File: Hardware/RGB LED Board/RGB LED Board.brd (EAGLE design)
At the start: 38.1 x 18.7 mm, 9 parts, among them U1 WS2801

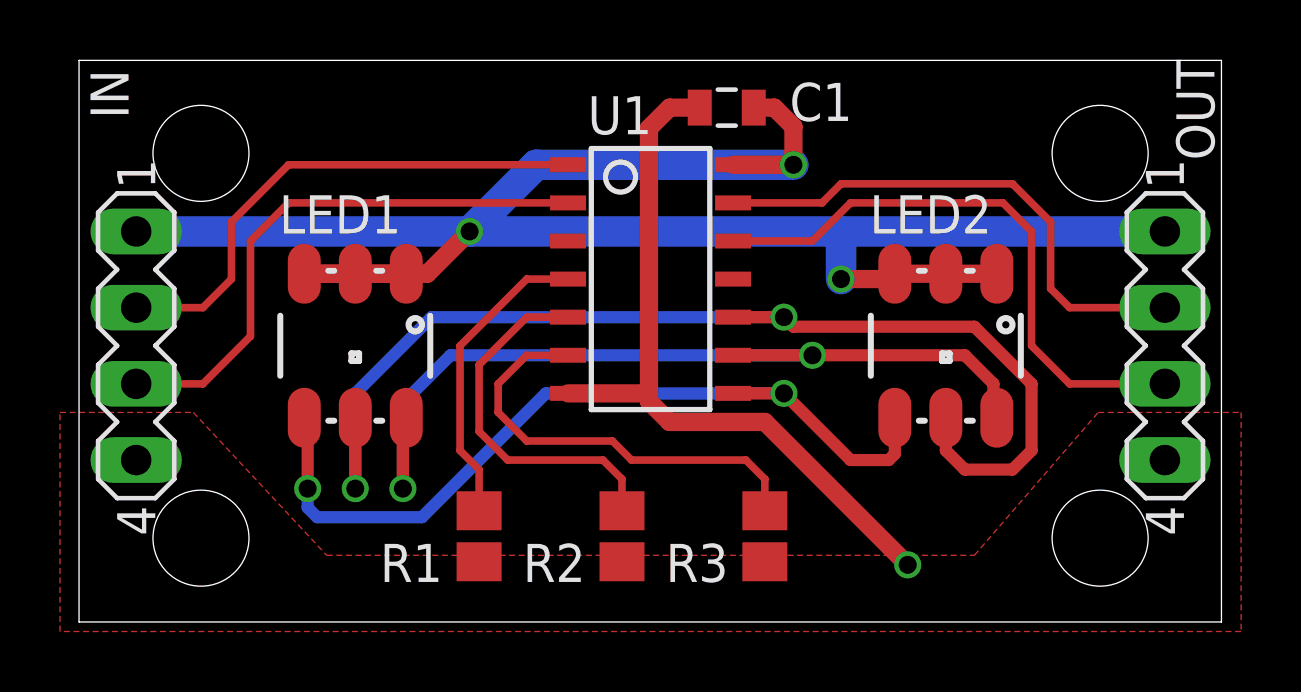
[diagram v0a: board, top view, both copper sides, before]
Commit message: changed LED to CLY6D-FKC-CK1N1D1BB7D3D3
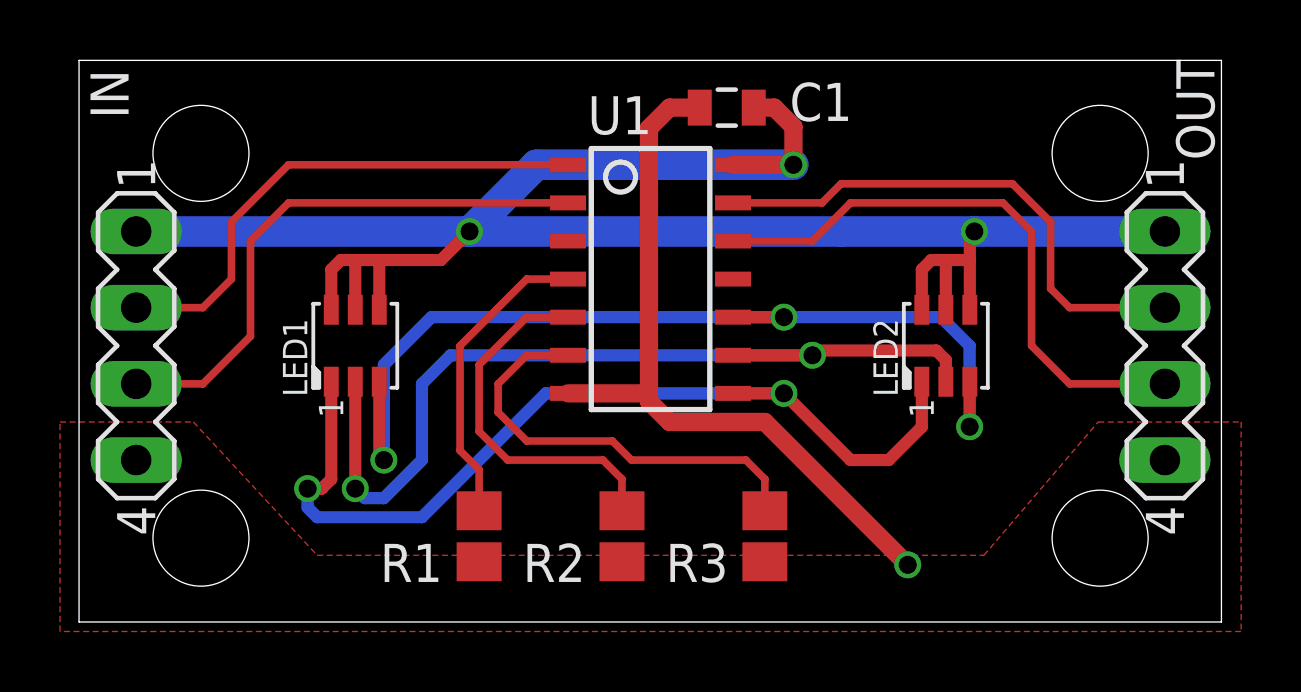
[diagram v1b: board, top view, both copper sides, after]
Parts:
- LED1, LED2: value LED-TRICOLOR-5050NO_IC -> CLY6D-FKC-CK1N1D1BB7D3D3; device SparkFun-LED:LED-TRICOLOR-5050 -> PP_LED:CLY6D-FKC
- R1: value 15 -> 20
- R2, R3: value 15 -> 30
- turned LED1 to 90 degrees
- turned LED2 to 90 degrees
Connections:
- net 456456456 renamed RFB
- net BG renamed BFB
- net GG renamed GFB
- net +5V: now also LED1.P$4, LED1.P$5, LED1.P$6, LED2.P$4, LED2.P$5, LED2.P$6; no longer LED1.1, LED1.2, LED1.3, LED2.1, LED2.2, LED2.3
- net B: now also LED1.P$1, LED2.P$1; no longer LED1.4, LED2.4
- net G: now also LED1.P$2, LED2.P$2; no longer LED1.6, LED2.6
- net R: now also LED1.P$3, LED2.P$3; no longer LED1.5, LED2.5
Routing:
- net R: track 38.4 -> 32.3 mm, vias 2 -> 3
- net B: track 28.4 -> 31.7 mm
- net +5V: track 67.4 -> 68.1 mm
